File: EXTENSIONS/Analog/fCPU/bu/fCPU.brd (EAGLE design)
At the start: 97 x 70 mm, 19 parts

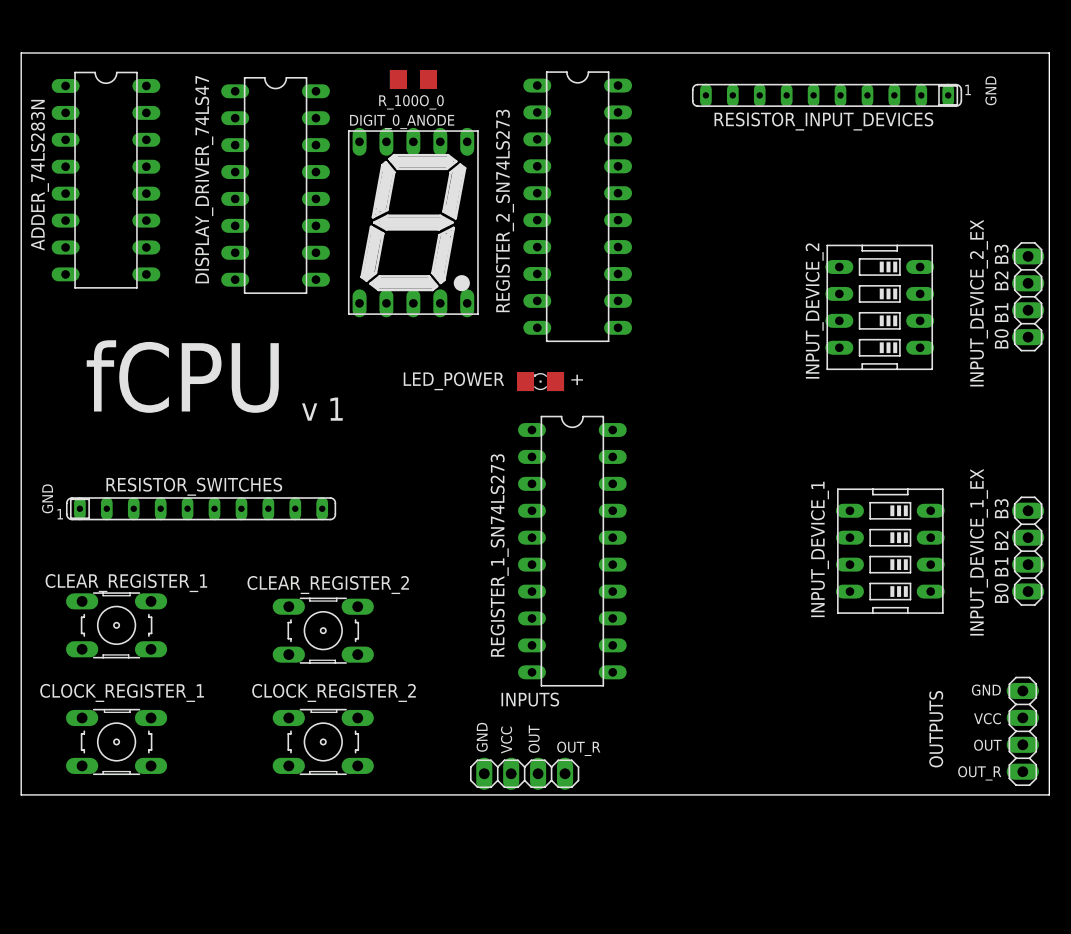
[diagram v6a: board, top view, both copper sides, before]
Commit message: Added old pcb deleted by accident
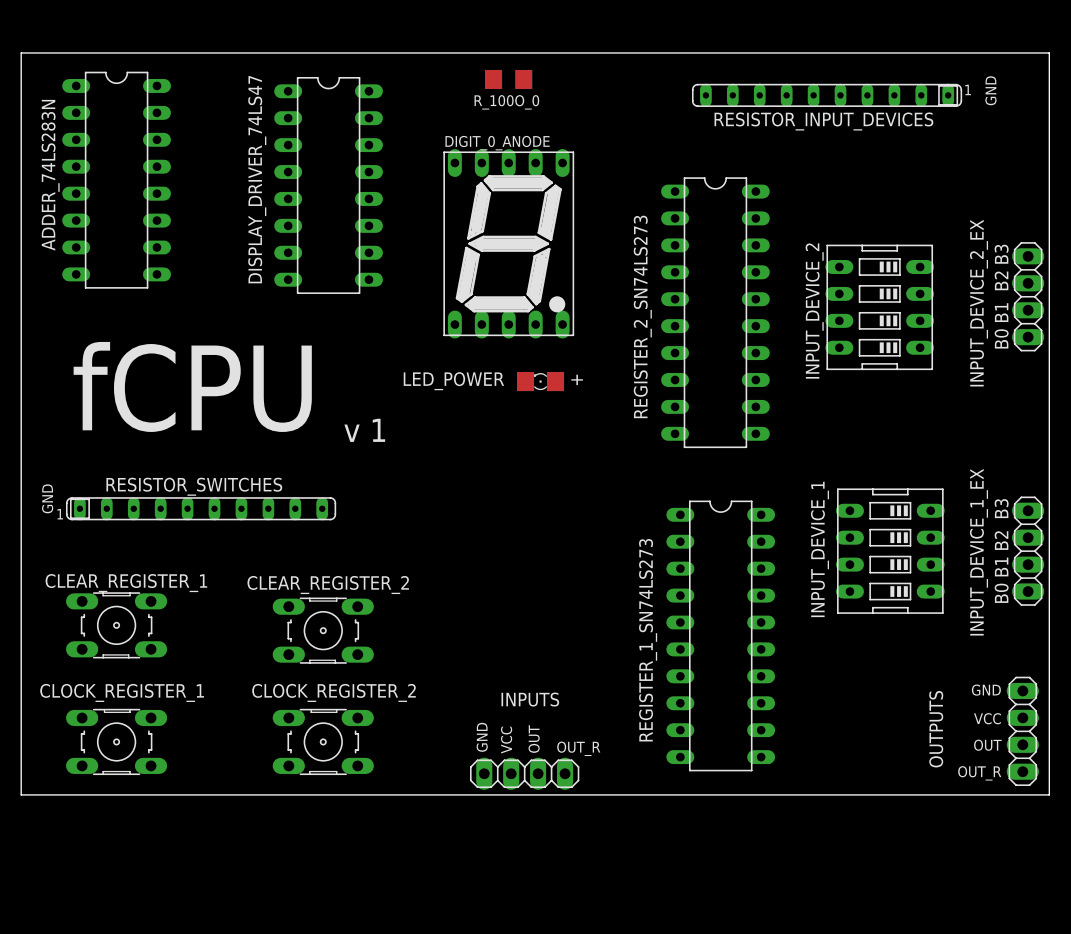
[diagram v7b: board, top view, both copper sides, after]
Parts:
- moved REGISTER_2_SN74LS273 16.4 mm to (67.5, 57.5)
- moved REGISTER_1_SN74LS273 16.1 mm to (68.0, 27.0)
- moved DIGIT_0_ANODE 9.22 mm to (48.0, 64.0)
- moved R_100O_0 9.00 mm to (48.0, 79.5)
- moved DISPLAY_DRIVER_74LS47 5.00 mm to (31.0, 69.5)
- moved ADDER_74LS283N 1.00 mm to (11.0, 70.0)
